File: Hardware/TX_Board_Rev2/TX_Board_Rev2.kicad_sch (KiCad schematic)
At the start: 43 parts, among them IC1 GP2Y1+, IC2 GP2Y1+, IC24 ADP5600ACPZ-R7, IC25 TPS7A4701RGWT, IC27 ADPL40502AUJZ-1.8-R7, IC3 GP2Y1+, J10 MM8030-2610RJ3, J11 MM8030-2610RJ3, J12 MM8030-2610RJ3, J18 Conn_01x08, J19 694106301002, J20 CONSMA022-G, J9 MM8030-2610RJ3, U1 SN74HCT138NSR

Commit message: Rev 3, rotated interface connectors
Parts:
- renumbered D1 to DEVICE_ID1, J9 to J4, J10 to J5, J11 to J6, J12 to J7, IC27 to LDO_1V8, IC24 to LDO_NEG5, IC25 to LDO_POS5, J20 to RF_IN1
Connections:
- net ATTN_LE_0: now also R3.1; no longer R5.2
- net ATTN_LE_1: now also R5.2; no longer R6.2
- net ATTN_LE_2: now also R6.2; no longer R7.2
- net ATTN_LE_3: now also R7.2; no longer R8.2
- net GPIO-G1: now also JP1.4; no longer JP1.7
- net GPIOA: now also JP1.7; no longer JP1.4
- net GPIOB: now also JP1.6; no longer JP1.5
- net GPIOC: now also JP1.5; no longer JP1.6
- net PS_LE_0: now also R8.2; no longer R3.1
- net PS_LE_1: now also R9.2; no longer R11.2
- net PS_LE_3: now also R11.2; no longer R9.2
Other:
- note added: "Debug headers"
- moved on the sheet: J18

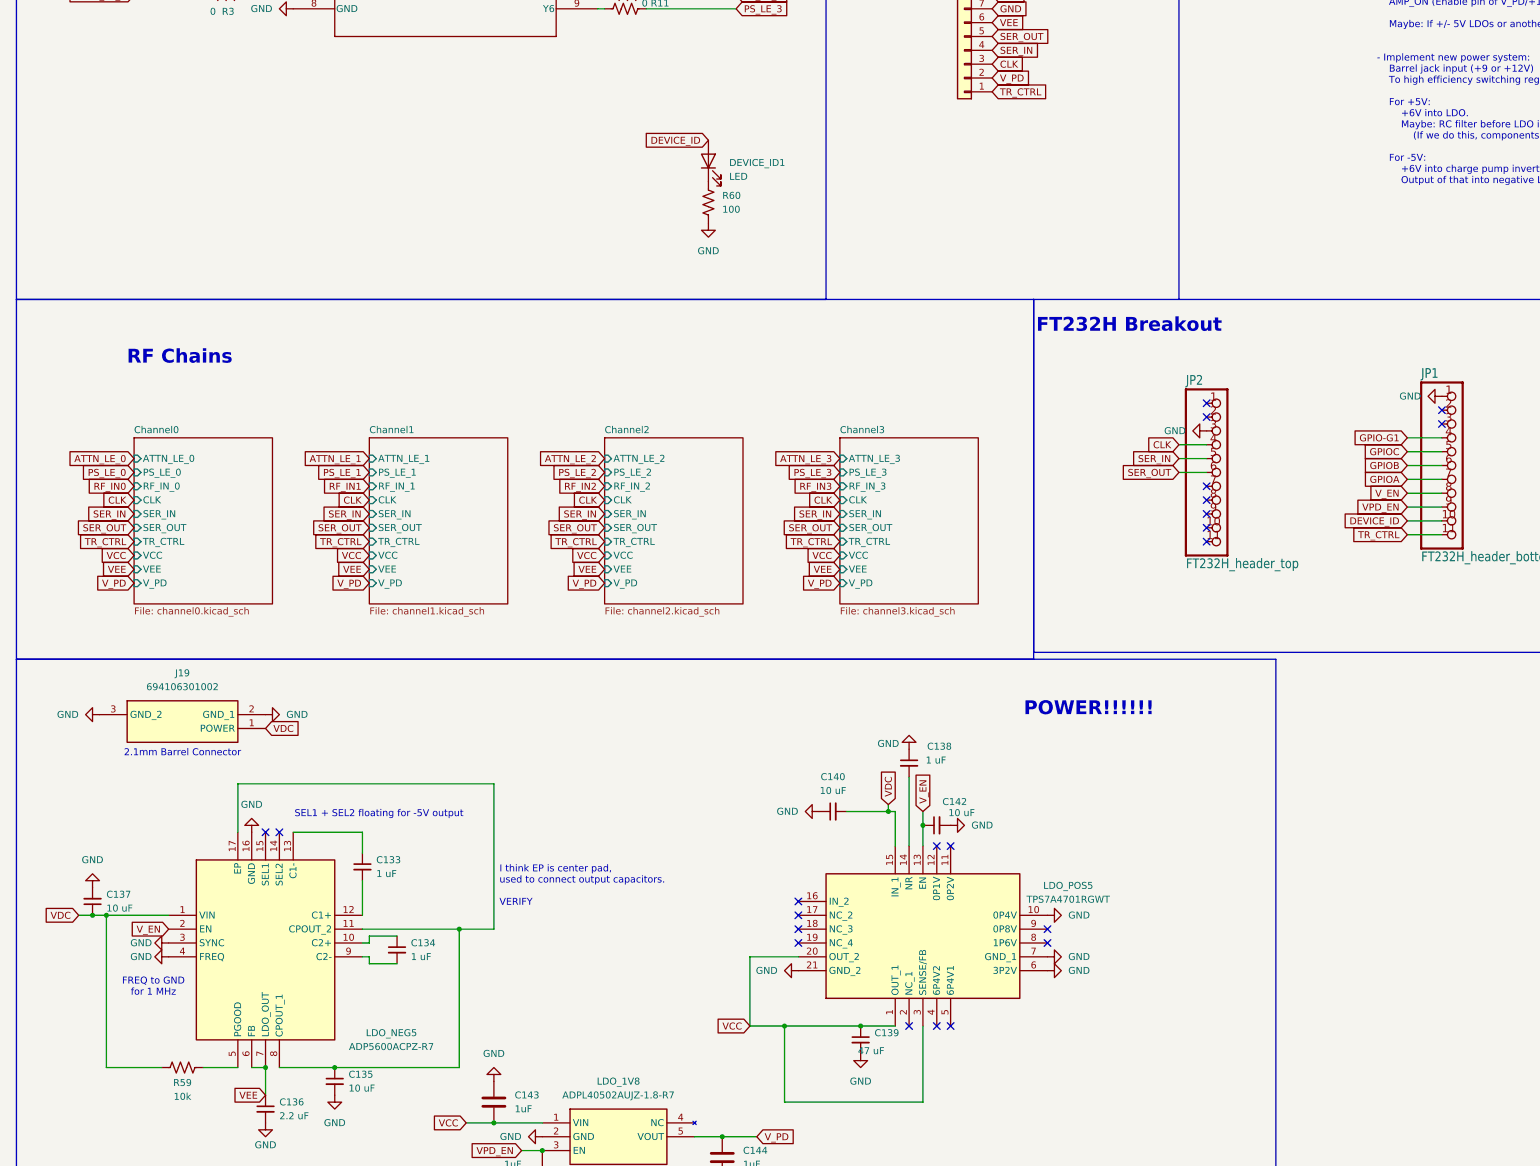
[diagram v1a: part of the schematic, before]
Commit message: optimal radiation patterns + a few rev 3 fixes
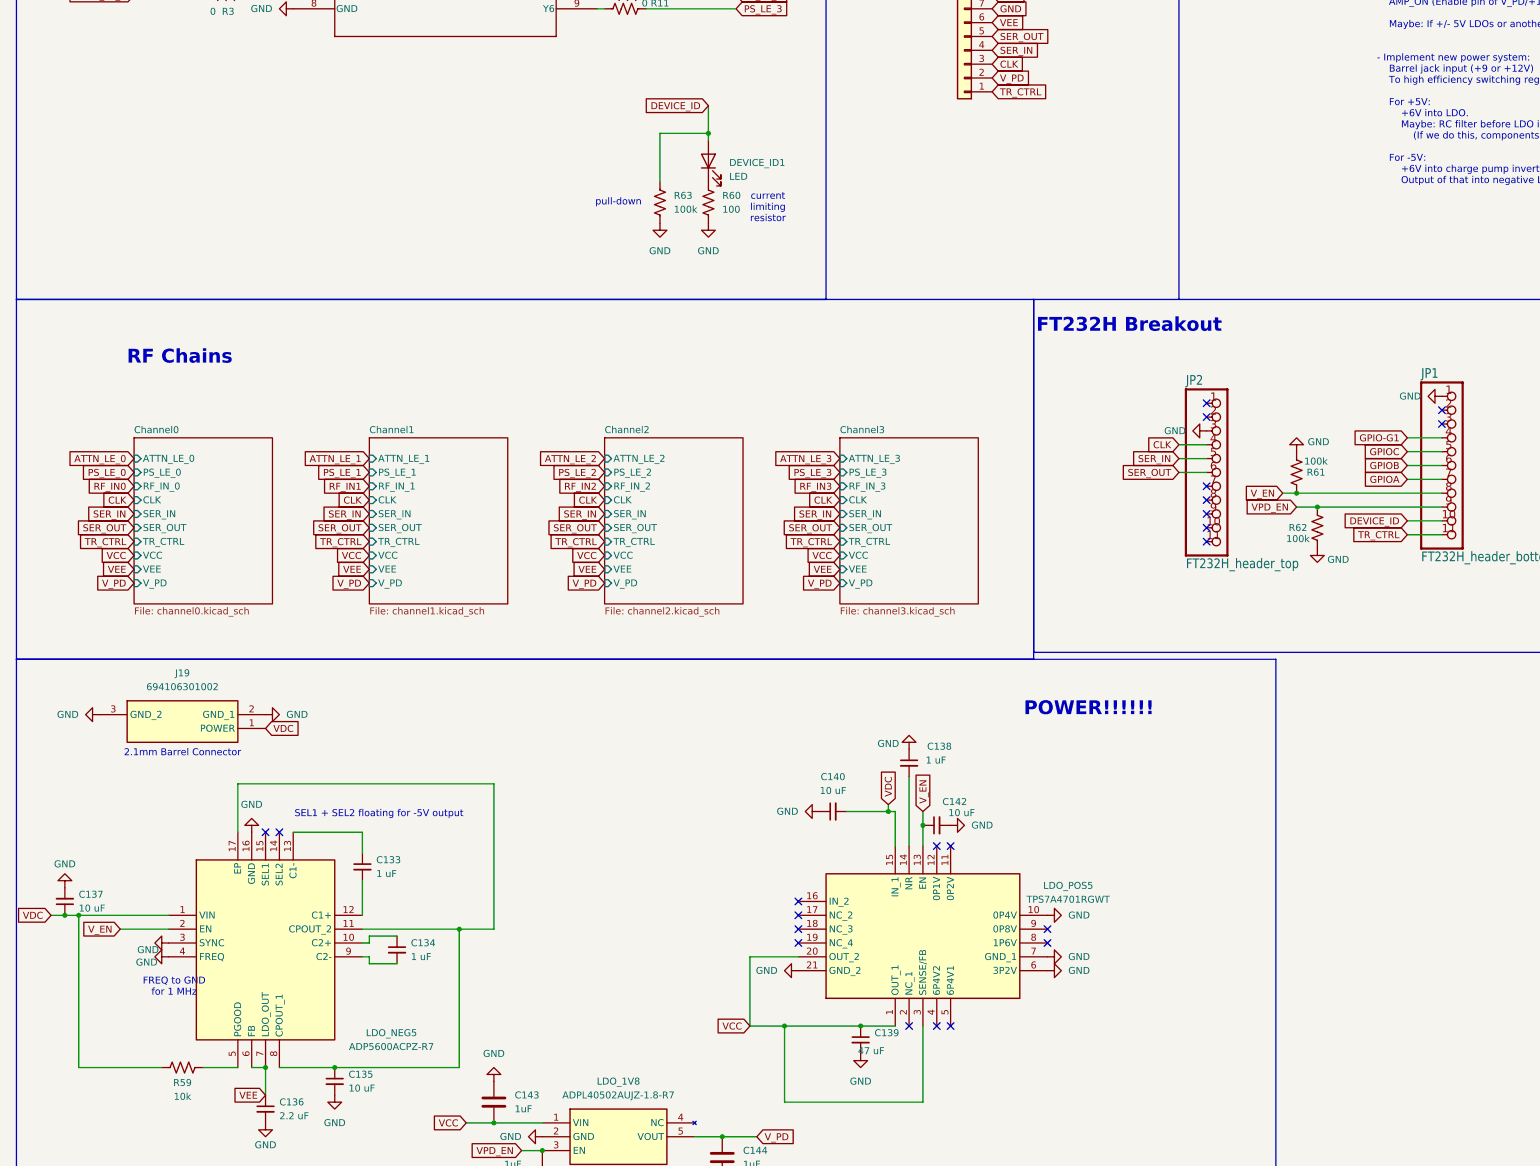
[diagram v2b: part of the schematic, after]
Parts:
- added R61, R62, R63: 100k, Resistor_SMD:R_0402_1005Metric, symbol Device:R_US
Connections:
- net DEVICE_ID: now also R63.1
- net GND: now also R61.1, R62.1, R63.2
- net VPD_EN: now also R62.2
- net V_EN: now also R61.2
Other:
- note added: "current limiting resistor"
- note added: "pull-down"
- note removed: "I think EP is center pad, used to connect output capacitors. VERIFY"
- moved on the sheet: C137

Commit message: User guide
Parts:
- added APT2012LSECK/J3-PRV1: LED, LED_SMD:LED_0805_2012Metric, symbol Device:LED
- added CR1: BZT52C2V4S-7-F, BZT52C2V4S_7_F:SOD323_DIO, symbol BZT52C2V4S:BZT52C2V4S-7-F
- added R64: 300, Resistor_SMD:R_0402_1005Metric, symbol Device:R_US
- added R65, R66: 100k, Resistor_SMD:R_0402_1005Metric, symbol Device:R_US
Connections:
- net GND: now also R64.2, R65.1, R66.1
- net GPIO-G1: now also R66.2
- net TR_CTRL: now also R65.2
- net VCC: now also CR1.1
- new net: APT2012LSECK/J3-PRV1.1 (K), R64.1
- new net: APT2012LSECK/J3-PRV1.2 (A), CR1.2
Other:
- note removed: "TODO: - Implement FT232H with SPI capibility (CLK, SER_IN, SER_OUT) FT232H has its own chip select (CS) line as well. Probably driven internally by onboard SPI controller. (Not sure, verify) This could be used for pin G1A of the decoder to save a GPIO Need to determine which parts of the example schematic need to be kept - Implement and label the following GPIO's on the FT232H: GPIO 0-3 (CS decod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"

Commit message: Restored broken Rev 2 for posterity and cleaned up naming
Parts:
- removed APT2012LSECK/J3-PRV1: LED, LED_SMD:LED_0805_2012Metric, symbol Device:LED
- removed CR1: BZT52C2V4S-7-F, BZT52C2V4S_7_F:SOD323_DIO, symbol BZT52C2V4S:BZT52C2V4S-7-F
- removed R61, R62, R63, R65, R66: 100k, Resistor_SMD:R_0402_1005Metric, symbol Device:R_US
- removed R64: 300, Resistor_SMD:R_0402_1005Metric, symbol Device:R_US
- JP1, JP2: footprint Connector_PinHeader_2.54mm:PinHeader_1x11_P2.54mm_Vertical -> Connector_PinSocket_2.54mm:PinSocket_1x11_P2.54mm_Vertical
- renumbered DEVICE_ID1 to D1, LDO_NEG5 to IC24, LDO_POS5 to IC25, LDO_1V8 to IC27, J5 to J10, J6 to J11, J7 to J12, RF_IN1 to J20, J4 to J9
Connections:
- net ATTN_LE_0: now also R5.2; no longer R3.1
- net ATTN_LE_1: now also R6.2; no longer R5.2
- net ATTN_LE_2: now also R7.2; no longer R6.2
- net ATTN_LE_3: now also R8.2; no longer R7.2
- net CLK: now also JP1.4; no longer JP2.4
- net DEVICE_ID: now also JP2.7; no longer JP1.10
- net GND: now also JP1.3; no longer JP1.1, JP2.3
- net PS_LE_0: now also R3.1; no longer R8.2
- net PS_LE_1: now also R11.2; no longer R9.2
- net PS_LE_3: now also R9.2; no longer R11.2
- net SER_IN: now also JP1.5; no longer JP2.5
- net SER_OUT: now also JP1.6; no longer JP2.6
- net TR_CTRL: now also JP2.4; no longer JP1.11
- net VPD_EN: now also JP2.6; no longer JP1.9
- net V_EN: now also JP2.5; no longer JP1.8
- net GPIO1: now reaches JP2.1
- net GPIO1: now also U1.1 (A)
- net GPIO2: now reaches JP2.2
- net GPIO2: now also U1.2 (B)
- net GPIO-G1 renamed GPIO0
- net GPIO0: no longer JP1.4
- net GPIOA: no longer names the net of JP1.7
- net GPIOA: no longer U1.1 (A)
- removed net GPIOB: JP1.6, U1.2 (B)
- net GPIOC renamed GPIO3
- net GPIO3: now also JP2.3; no longer JP1.5
- no-connect marks 22 -> 24
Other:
- note added: "I think EP is center pad, used to connect output capacitors. VERIFY"
- note added: "TODO: - Implement FT232H with SPI capibility (CLK, SER_IN, SER_OUT) FT232H has its own chip select (CS) line as well. Probably driven internally by onboard SPI controller. (Not sure, verify) This could be used for pin G1A of the decoder to save a GPIO Need to determine which parts of the example schematic need to be kept - Implement and label the following GPIO's on the FT232H: GPIO 0-3 (CS decod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"
- note removed: "Debug headers"
- note removed: "current limiting resistor"
- note removed: "pull-down"
- moved on the sheet: C137, J18
